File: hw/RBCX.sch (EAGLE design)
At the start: 470 parts, among them IC1 AMS1117-3.3, IC10 INA180A4, IC11 INA180A4, IC12 MPU-6050, IC13 STM32F103VCT6, IC2 DRV8833PWP, IC3 INA180A4, IC4 INA180A4, IC5 DRV8833PWP, IC6 INA180A4, IC7 INA180A4, IC8 INA180A4, IC9 INA180A4, P1 M1, P2 M2, P3 M3, P4 M4, Q1 NCE20P45Q, Q10 2N7002, Q2 NCE20P45Q, Q3 2N7002, Q4 2N7002, Q5 2N7002, Q6 2N7002, Q7 2N7002, Q8 2N7002, Q9 2N7002, X1 POWER_IN, X2 POWER_OUT, X3 52559-3092, X4 uUSB, Y1 5032/2P, Y2 3215_2P

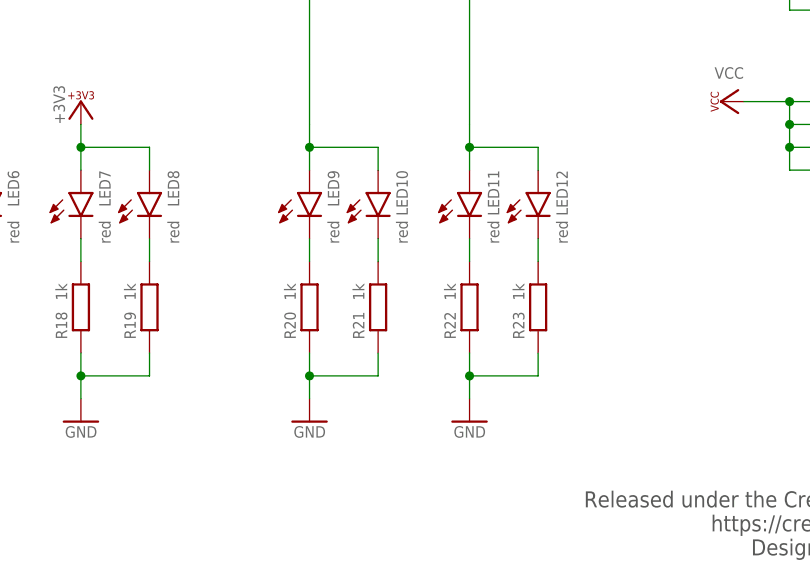
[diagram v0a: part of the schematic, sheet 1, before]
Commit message: hw: change resistors R20 - R23 valu to 2k2 (VUSB and ESP_+5V power LED resistors)
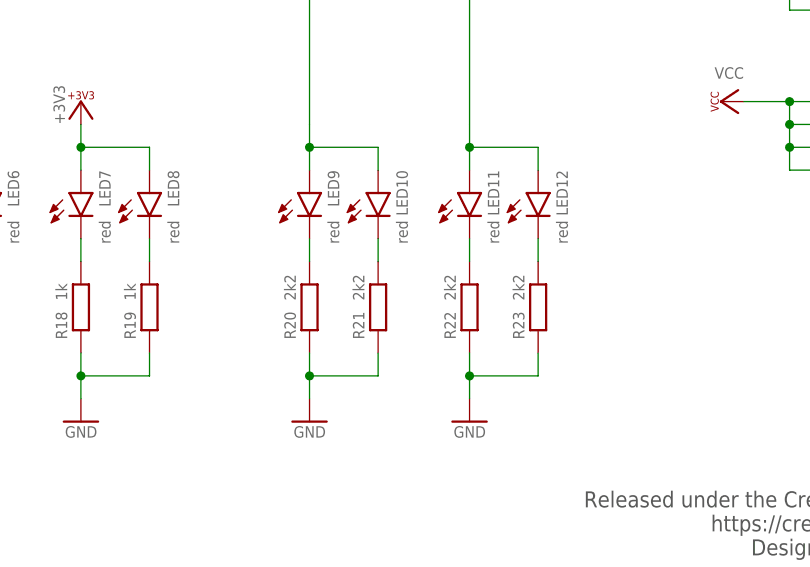
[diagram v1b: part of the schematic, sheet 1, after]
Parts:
- R20, R21, R22, R23: value 1k -> 2k2
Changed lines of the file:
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@@
 <part name="LED22" library="led" deviceset="LED" device="CHIPLED_0603" package3d_urn="urn:adsk.eagle:package:15822/2" value="red"/>
 <part name="LED24" library="led" deviceset="LED" device="CHIPLED_0603" package3d_urn="urn:adsk.eagle:package:15822/2" value="red"/>
-<part name="R20" library="rcl_upravena" deviceset="R-EU_" device="R0402" value="1k"/>
+<part name="R20" library="rcl_upravena" deviceset="R-EU_" device="R0402" value="2k2"/>
 <part name="GND47" library="Supply" deviceset="GND" device=""/>
-<part name="R22" library="rcl_upravena" deviceset="R-EU_" device="R0402" value="1k"/>
+<part name="R22" library="rcl_upravena" deviceset="R-EU_" device="R0402" value="2k2"/>
 <part name="GND48" library="Supply" deviceset="GND" device=""/>
 <part name="LED9" library="led" deviceset="LED" device="CHIPLED_0603" package3d_urn="urn:adsk.eagle:package:15822/2" value="red"/>
 <part name="LED11" library="led" deviceset="LED" device="CHIPLED_0603" package3d_urn="urn:adsk.eagle:package:15822/2" value="red"/>
-<part name="R21" library="rcl_upravena" deviceset="R-EU_" device="R0402" value="1k"/>
-<part name="R23" library="rcl_upravena" deviceset="R-EU_" device="R0402" value="1k"/>
+<part name="R21" library="rcl_upravena" deviceset="R-EU_" device="R0402" value="2k2"/>
+<part name="R23" library="rcl_upravena" deviceset="R-EU_" device="R0402" value="2k2"/>
 <part name="LED10" library="led" deviceset="LED" device="CHIPLED_0603" package3d_urn="urn:adsk.eagle:package:15822/2" value="red"/>
 <part name="LED12" library="led" deviceset="LED" device="CHIPLED_0603" package3d_urn="urn:adsk.eagle:package:15822/2" value="red"/>

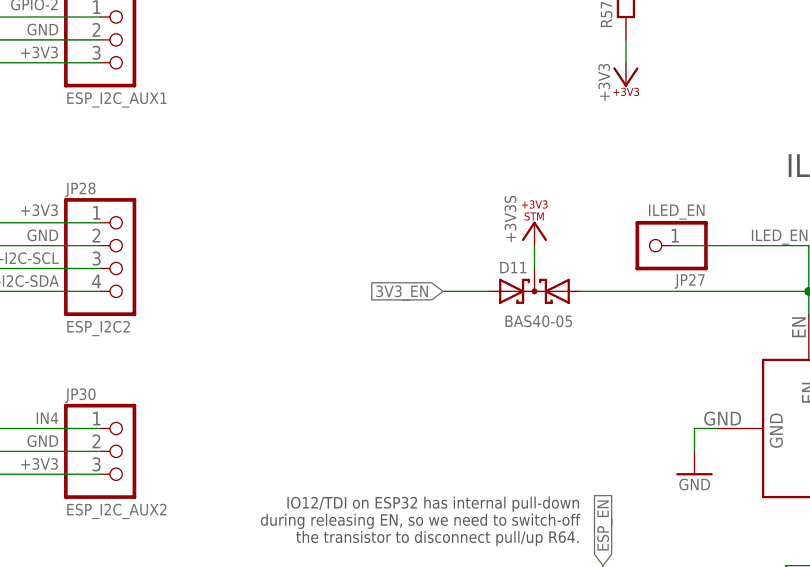
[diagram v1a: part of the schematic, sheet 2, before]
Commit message: hw: disconnect 3V3_EN and D11 (this connection prevents main step-down IM1 from startup)
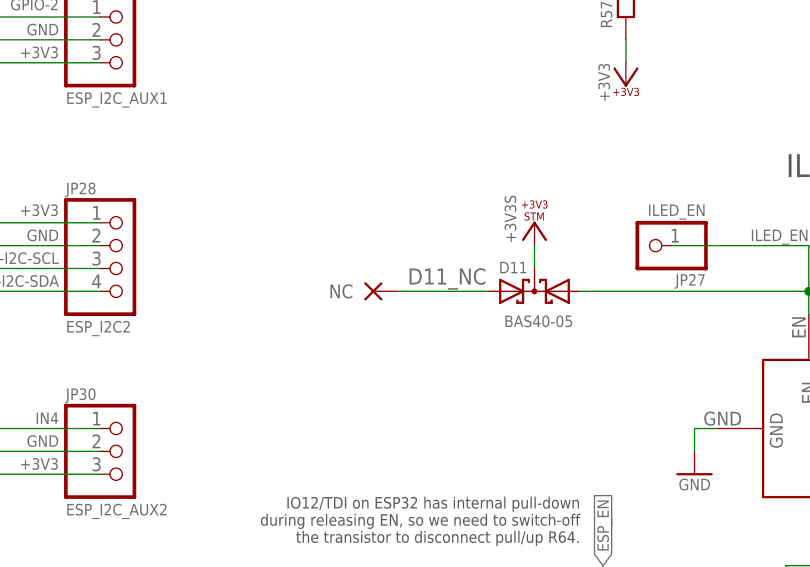
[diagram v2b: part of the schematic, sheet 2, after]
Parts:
- added NC7: NC, NC:NC
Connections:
- new net D11_NC: D11.A2, NC7.NC
- net 3V3_EN: no longer D11.A2
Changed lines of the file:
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@@
 <part name="R107" library="rcl_upravena" deviceset="R-EU_" device="R0402" value="1M"/>
 <part name="JP35" library="pinhead" library_urn="urn:adsk.eagle:library:325" deviceset="PINHD-1X4" device="" package3d_urn="urn:adsk.eagle:package:22407/2" value="USBC_AUX"/>
+<part name="NC7" library="NC" deviceset="NC" device=""/>
 </parts>
 <sheets>
@@
 <attribute name="VALUE" x="160.528" y="78.994" size="1.27" layer="96" rot="R90"/>
 </instance>
+<instance part="NC7" gate="G$1" x="147.32" y="73.66" smashed="yes" rot="R180"/>
 </instances>
 <busses>
@@
 </segment>
 </net>
-<net name="3V3_EN" class="0">
+<net name="D11_NC" class="0">
 <segment>
+<wire x1="157.48" y1="73.66" x2="147.32" y2="73.66" width="0.1524" layer="91"/>
+<pinref part="NC7" gate="G$1" pin="NC"/>
 <pinref part="D11" gate="G$1" pin="A2"/>
-<wire x1="157.48" y1="73.66" x2="152.4" y2="73.66" width="0.1524" layer="91"/>
-<label x="152.4" y="73.66" size="1.27" layer="95" rot="R180" xref="yes"/>
+<label x="157.226" y="74.422" size="1.778" layer="95" rot="MR0"/>
 </segment>
 </net>

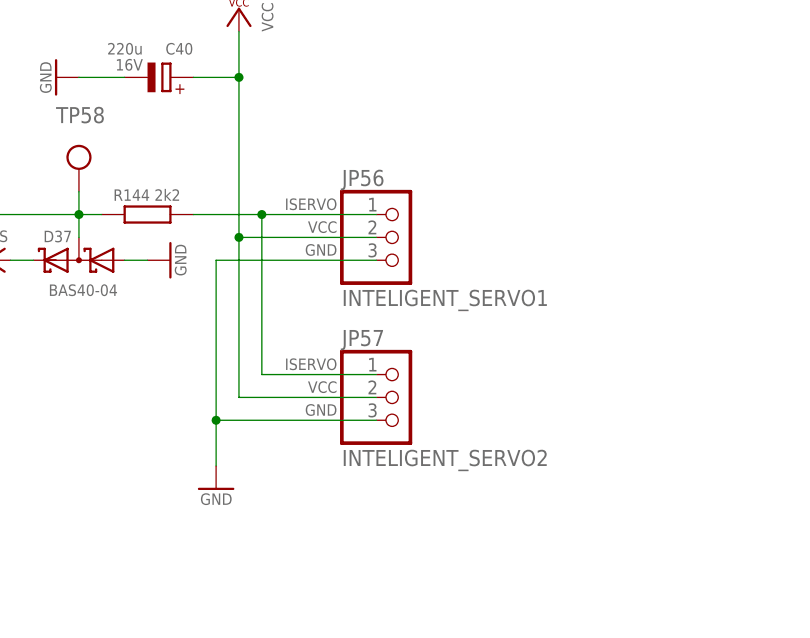
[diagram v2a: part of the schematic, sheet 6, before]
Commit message: hw: fix jst connectors drill (motor connectors) and pad size (iServo connectors), move bottom pinheads to left to make enough space for iServo connectors
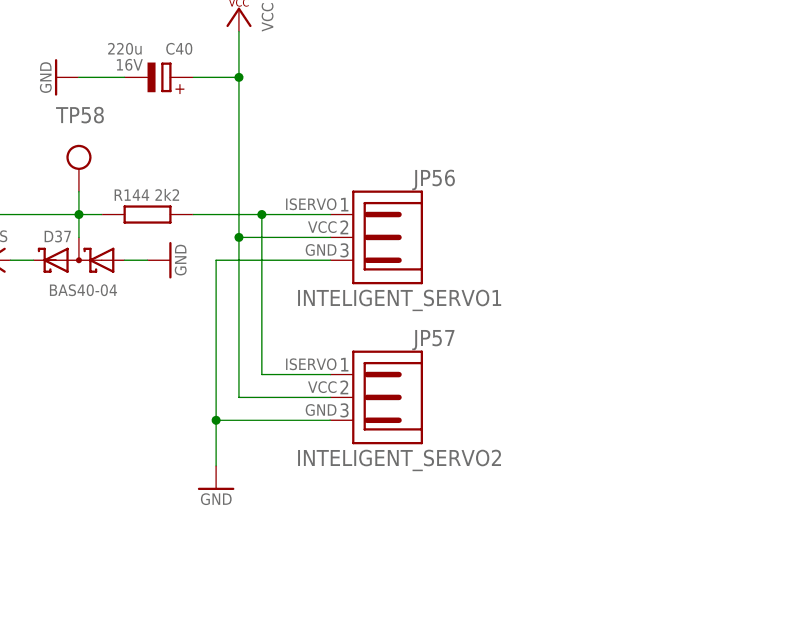
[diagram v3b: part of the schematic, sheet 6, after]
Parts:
- JP56, JP57: device iServo_connector:292161-3 -> jst-ph:JST-PH3
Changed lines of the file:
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@@
 <part name="NC5" library="NC" deviceset="NC" device=""/>
 <part name="NC6" library="NC" deviceset="NC" device=""/>
-<part name="JP56" library="iServo_connector" deviceset="292161-3" device="" value="INTELIGENT_SERVO1">
+<part name="JP56" library="jst-ph" deviceset="JST-PH3" device="" value="INTELIGENT_SERVO1">
 <attribute name="DESCRIPTION" value="Connector for inteligent servo LewanSoul (e.g. LX-15D)"/>
 <attribute name="PACKAGE" value="292161-3"/>
@@
 <part name="IC5" library="DRV8833" deviceset="DRV8833" device="PWP" value="DRV8833PWP"/>
 <part name="SJ9" library="jumper" deviceset="SJ2W_DEFAULT" device=""/>
-<part name="JP57" library="iServo_connector" deviceset="292161-3" device="" value="INTELIGENT_SERVO2">
+<part name="JP57" library="jst-ph" deviceset="JST-PH3" device="" value="INTELIGENT_SERVO2">
 <attribute name="DESCRIPTION" value="Connector for inteligent servo LewanSoul (e.g. LX-15D)"/>
 <attribute name="PACKAGE" value="292161-3"/>
@@
 </plain>
 <instances>
-<instance part="JP56" gate="G$1" x="104.14" y="58.42" smashed="yes">
-<attribute name="NAME" x="97.79" y="64.135" size="1.778" layer="95"/>
-<attribute name="VALUE" x="97.79" y="50.8" size="1.778" layer="96"/>
-<attribute name="DESCRIPTION" x="104.14" y="58.42" size="1.778" layer="96" display="off"/>
-<attribute name="PACKAGE" x="104.14" y="58.42" size="1.778" layer="96" display="off"/>
-</instance>
-<instance part="JP57" gate="G$1" x="104.14" y="40.64" smashed="yes">
-<attribute name="NAME" x="97.79" y="46.355" size="1.778" layer="95"/>
-<attribute name="VALUE" x="97.79" y="33.02" size="1.778" layer="96"/>
-<attribute name="DESCRIPTION" x="104.14" y="40.64" size="1.778" layer="96" display="off"/>
-<attribute name="PACKAGE" x="104.14" y="40.64" size="1.778" layer="96" display="off"/>
+<instance part="JP56" gate="G$1" x="104.14" y="58.42" smashed="yes" rot="MR0">
+<attribute name="NAME" x="110.49" y="64.135" size="1.778" layer="95" rot="MR0"/>
+<attribute name="VALUE" x="92.71" y="50.8" size="1.778" layer="96"/>
+<attribute name="DESCRIPTION" x="104.14" y="58.42" size="1.778" layer="96" rot="MR0" display="off"/>
+<attribute name="PACKAGE" x="104.14" y="58.42" size="1.778" layer="96" rot="MR0" display="off"/>
+</instance>
+<instance part="JP57" gate="G$1" x="104.14" y="40.64" smashed="yes" rot="MR0">
+<attribute name="NAME" x="110.49" y="46.355" size="1.778" layer="95" rot="MR0"/>
+<attribute name="VALUE" x="92.71" y="33.02" size="1.778" layer="96"/>
+<attribute name="DESCRIPTION" x="104.14" y="40.64" size="1.778" layer="96" rot="MR0" display="off"/>
+<attribute name="PACKAGE" x="104.14" y="40.64" size="1.778" layer="96" rot="MR0" display="off"/>
 </instance>
 <instance part="FRAME5" gate="G$1" x="0" y="0" smashed="yes">
@@
 <pinref part="JP56" gate="G$1" pin="3"/>
 <pinref part="GND78" gate="1" pin="GND"/>
-<wire x1="101.6" y1="55.88" x2="83.82" y2="55.88" width="0.1524" layer="91"/>
+<wire x1="96.52" y1="55.88" x2="83.82" y2="55.88" width="0.1524" layer="91"/>
 <wire x1="83.82" y1="55.88" x2="83.82" y2="38.1" width="0.1524" layer="91"/>
 <pinref part="JP57" gate="G$1" pin="3"/>
 <wire x1="83.82" y1="38.1" x2="83.82" y2="33.02" width="0.1524" layer="91"/>
-<wire x1="101.6" y1="38.1" x2="83.82" y2="38.1" width="0.1524" layer="91"/>
+<wire x1="96.52" y1="38.1" x2="83.82" y2="38.1" width="0.1524" layer="91"/>
 <junction x="83.82" y="38.1"/>
 <label x="97.282" y="38.608" size="1.27" layer="95" rot="MR0"/>
@@
 <pinref part="JP57" gate="G$1" pin="2"/>
 <pinref part="P+22" gate="VCC" pin="VCC"/>
-<wire x1="101.6" y1="40.64" x2="86.36" y2="40.64" width="0.1524" layer="91"/>
+<wire x1="96.52" y1="40.64" x2="86.36" y2="40.64" width="0.1524" layer="91"/>
 <wire x1="86.36" y1="40.64" x2="86.36" y2="58.42" width="0.1524" layer="91"/>
 <pinref part="JP56" gate="G$1" pin="2"/>
 <wire x1="86.36" y1="58.42" x2="86.36" y2="76.2" width="0.1524" layer="91"/>
 <wire x1="86.36" y1="76.2" x2="86.36" y2="81.28" width="0.1524" layer="91"/>
-<wire x1="101.6" y1="58.42" x2="86.36" y2="58.42" width="0.1524" layer="91"/>
+<wire x1="96.52" y1="58.42" x2="86.36" y2="58.42" width="0.1524" layer="91"/>
 <junction x="86.36" y="58.42"/>
 <label x="97.282" y="41.148" size="1.27" layer="95" rot="MR0"/>
@@
 <wire x1="81.28" y1="60.96" x2="88.9" y2="60.96" width="0.1524" layer="91"/>
 <pinref part="JP57" gate="G$1" pin="1"/>
-<wire x1="88.9" y1="60.96" x2="101.6" y2="60.96" width="0.1524" layer="91"/>
-<wire x1="101.6" y1="43.18" x2="88.9" y2="43.18" width="0.1524" layer="91"/>
+<wire x1="88.9" y1="60.96" x2="96.52" y2="60.96" width="0.1524" layer="91"/>
+<wire x1="96.52" y1="43.18" x2="88.9" y2="43.18" width="0.1524" layer="91"/>
 <wire x1="88.9" y1="43.18" x2="88.9" y2="60.96" width="0.1524" layer="91"/>
 <junction x="88.9" y="60.96"/>

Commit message: hw: fix USB-C CC pin pull-down resistors value.
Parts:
- R76, R77: value 1k -> 5k1
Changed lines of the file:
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@@
 <part name="GND157" library="Supply" deviceset="GND" device=""/>
 <part name="GND163" library="Supply" deviceset="GND" device=""/>
-<part name="R76" library="rcl_upravena" deviceset="R-EU_" device="R0402" value="1k"/>
-<part name="R77" library="rcl_upravena" deviceset="R-EU_" device="R0402" value="1k"/>
+<part name="R76" library="rcl_upravena" deviceset="R-EU_" device="R0402" value="5k1"/>
+<part name="R77" library="rcl_upravena" deviceset="R-EU_" device="R0402" value="5k1"/>
 <part name="TP61" library="test_points" deviceset="TP" device="_06MM"/>
 <part name="TP13" library="test_points" deviceset="TP" device="_06MM"/>

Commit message: hw: add buttons value
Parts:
- S1, S10, S11, S12, S13, S14, S2, S3, S4, S5, S6, S7, S8, S9: value CHOOSE_ME -> TS-1187A-C-C-B
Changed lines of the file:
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@@
 <attribute name="PACKAGE" value="292161-3"/>
 </part>
-<part name="S2" library="switch-omron" deviceset="10-XX" device="_SMD" value="CHOOSE_ME"/>
+<part name="S2" library="switch-omron" deviceset="10-XX" device="_SMD" value="TS-1187A-C-C-B"/>
 <part name="GND1" library="Supply" deviceset="GND" device=""/>
 <part name="GND2" library="Supply" deviceset="GND" device=""/>
@@
 <part name="R52" library="rcl_upravena" deviceset="R-EU_" device="R0402" value="330R"/>
 <part name="R53" library="rcl_upravena" deviceset="R-EU_" device="R0402" value="330R"/>
-<part name="S3" library="switch-omron" deviceset="10-XX" device="_SMD" value="CHOOSE_ME"/>
-<part name="S5" library="switch-omron" deviceset="10-XX" device="_SMD" value="CHOOSE_ME"/>
-<part name="S7" library="switch-omron" deviceset="10-XX" device="_SMD" value="CHOOSE_ME"/>
-<part name="S9" library="switch-omron" deviceset="10-XX" device="_SMD" value="CHOOSE_ME"/>
+<part name="S3" library="switch-omron" deviceset="10-XX" device="_SMD" value="TS-1187A-C-C-B"/>
+<part name="S5" library="switch-omron" deviceset="10-XX" device="_SMD" value="TS-1187A-C-C-B"/>
+<part name="S7" library="switch-omron" deviceset="10-XX" device="_SMD" value="TS-1187A-C-C-B"/>
+<part name="S9" library="switch-omron" deviceset="10-XX" device="_SMD" value="TS-1187A-C-C-B"/>
 <part name="R90" library="rcl_upravena" deviceset="R-EU_" device="R0402" value="330R"/>
 <part name="R93" library="rcl_upravena" deviceset="R-EU_" device="R0402" value="330R"/>
@@
 <part name="P+39" library="Supply" deviceset="+5V" device=""/>
 <part name="P+40" library="Supply" deviceset="VCC" device=""/>
-<part name="S11" library="switch-omron" deviceset="10-XX" device="_SMD" value="CHOOSE_ME"/>
+<part name="S11" library="switch-omron" deviceset="10-XX" device="_SMD" value="TS-1187A-C-C-B"/>
 <part name="+3V60" library="Supply" deviceset="+3V3S" device=""/>
 <part name="R75" library="rcl_upravena" deviceset="R-EU_" device="R0402" value="100k"/>
@@
 <part name="+3V69" library="Supply" deviceset="+3V3S" device=""/>
 <part name="D12" library="diode" deviceset="SHOTTKY" device="-SMA" value="SS34"/>
-<part name="S13" library="switch-omron" deviceset="10-XX" device="_SMD" value="CHOOSE_ME"/>
+<part name="S13" library="switch-omron" deviceset="10-XX" device="_SMD" value="TS-1187A-C-C-B"/>
 <part name="GND151" library="supply1" library_urn="urn:adsk.eagle:library:371" deviceset="GND" device=""/>
 <part name="JP58" library="pinhead" library_urn="urn:adsk.eagle:library:325" deviceset="PINHD-2X2" device="" package3d_urn="urn:adsk.eagle:package:22455/2" value="I2C_INTERCONNECT"/>
@@
 <part name="X5" library="USB" deviceset="USB_C_8PIN" device=""/>
 <part name="GND33" library="Supply" deviceset="GND" device=""/>
-<part name="S4" library="switch-omron" deviceset="10-XX" device="_SMD" value="CHOOSE_ME"/>
-<part name="S6" library="switch-omron" deviceset="10-XX" device="_SMD" value="CHOOSE_ME"/>
-<part name="S8" library="switch-omron" deviceset="10-XX" device="_SMD" value="CHOOSE_ME"/>
-<part name="S10" library="switch-omron" deviceset="10-XX" device="_SMD" value="CHOOSE_ME"/>
-<part name="S12" library="switch-omron" deviceset="10-XX" device="_SMD" value="CHOOSE_ME"/>
-<part name="S14" library="switch-omron" deviceset="10-XX" device="_SMD" value="CHOOSE_ME"/>
-<part name="S1" library="switch-omron" deviceset="10-XX" device="_SMD" value="CHOOSE_ME"/>
+<part name="S4" library="switch-omron" deviceset="10-XX" device="_SMD" value="TS-1187A-C-C-B"/>
+<part name="S6" library="switch-omron" deviceset="10-XX" device="_SMD" value="TS-1187A-C-C-B"/>
+<part name="S8" library="switch-omron" deviceset="10-XX" device="_SMD" value="TS-1187A-C-C-B"/>
+<part name="S10" library="switch-omron" deviceset="10-XX" device="_SMD" value="TS-1187A-C-C-B"/>
+<part name="S12" library="switch-omron" deviceset="10-XX" device="_SMD" value="TS-1187A-C-C-B"/>
+<part name="S14" library="switch-omron" deviceset="10-XX" device="_SMD" value="TS-1187A-C-C-B"/>
+<part name="S1" library="switch-omron" deviceset="10-XX" device="_SMD" value="TS-1187A-C-C-B"/>
 <part name="C5" library="rcl_upravena" deviceset="C-EU" device="C0402" value="100n">
 <attribute name="DIELECTRIC" value="X5R"/>
